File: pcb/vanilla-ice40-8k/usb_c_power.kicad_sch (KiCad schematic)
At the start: 28 parts, among them J7 Conn_01x02_Pin, J8 Conn_01x02_Pin, J9 Conn_01x02_Pin, Q1 DMG2305UX-13, U5 TPS563252DRLR, U6 TPS563252DRLR

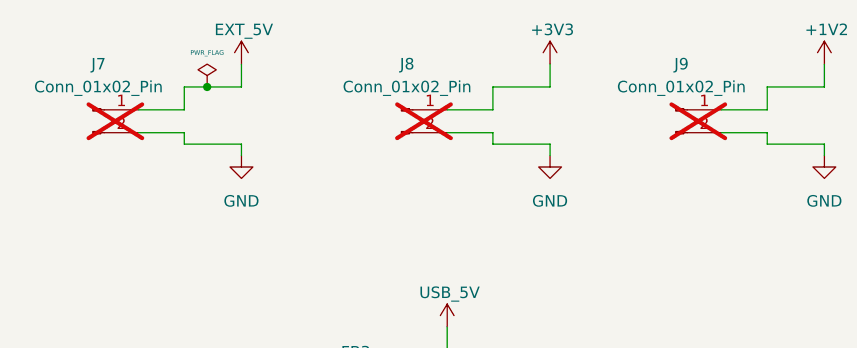
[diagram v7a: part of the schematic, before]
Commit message: [hx8k][pcb] updated J refs
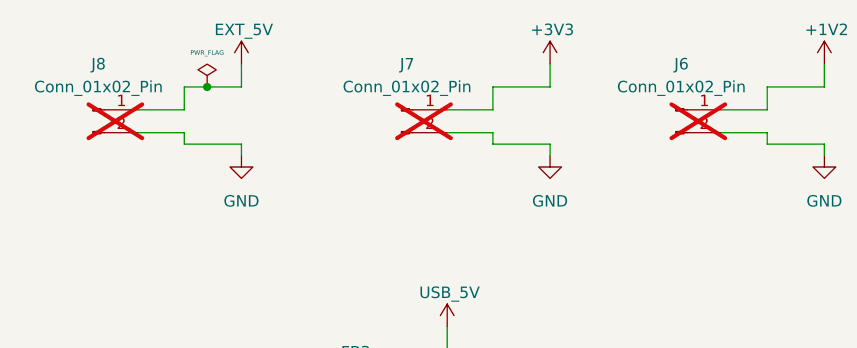
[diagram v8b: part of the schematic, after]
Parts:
- renumbered J9 to J6, J8 to J7, J7 to J8
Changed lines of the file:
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@@
 		(on_board yes)
 		(dnp yes)
-		(property "Reference" "J7"
+		(property "Reference" "J8"
 			(at 33.655 29.21 0)
 			(effects
@@
 			(project "vanilla-ice40-8k"
 				(path "/6fdfbf4b-014a-4077-8dc3-7ce5ecaf5fe5/4c09157d-3537-4cf3-bc9c-21379ec730e4"
-					(reference "J7")
+					(reference "J8")
 					(unit 1)
 				)
@@
 		(on_board yes)
 		(dnp yes)
-		(property "Reference" "J8"
+		(property "Reference" "J7"
 			(at 67.945 29.21 0)
 			(effects
@@
 			(project "vanilla-ice40-8k"
 				(path "/6fdfbf4b-014a-4077-8dc3-7ce5ecaf5fe5/4c09157d-3537-4cf3-bc9c-21379ec730e4"
-					(reference "J8")
+					(reference "J7")
 					(unit 1)
 				)
@@
 		(on_board yes)
 		(dnp yes)
-		(property "Reference" "J9"
+		(property "Reference" "J6"
 			(at 98.425 29.21 0)
 			(effects
@@
 			(project "vanilla-ice40-8k"
 				(path "/6fdfbf4b-014a-4077-8dc3-7ce5ecaf5fe5/4c09157d-3537-4cf3-bc9c-21379ec730e4"
-					(reference "J9")
-					(unit 1)
-				)
+					(reference "J6")
+					(unit 1)
+				)
